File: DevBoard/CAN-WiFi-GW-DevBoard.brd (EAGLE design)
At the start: 82.5 x 58.4 mm, 31 parts, among them J1 IN+, J2 OUT+, J3 IN-, J4 OUT-, J5 CAN_MODULE, SW1 CONFIGURATION, U1 74LVC1T45GW,125, U2 74LVC1T45GW,125, U3 74LVC1T45GW,125, X1 MKDSN1,5/2-5,08

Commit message: Fix labelling of config switches
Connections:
- net ESP_D6/LISTEN_MODE renamed ESP_D6/CAN_TX_EN
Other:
- board text added: "1 OTA 2 WRITE 3 CANTX 4 DEBUG"
- board text removed: "1 OTA 2 WRITE 3 LISTEN 4 DEBUG"
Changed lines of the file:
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@@
 <text x="56.8325" y="33.655" size="1.016" layer="21" font="vector" rot="R90" align="top-left">1 OTA
 2 WRITE
-3 LISTEN
+3 CANTX
 4 DEBUG</text>
 <text x="15.02" y="51.34" size="1.27" layer="21" font="vector" align="center">[dev. board]</text>
@@
 <wire x1="28.3152125" y1="44.1325" x2="24.13" y2="39.9472875" width="0.2032" layer="16"/>
 </signal>
-<signal name="ESP_D6/LISTEN_MODE">
+<signal name="ESP_D6/CAN_TX_EN">
 <contactref element="J8" pad="7"/>
 <contactref element="SW1" pad="3"/>

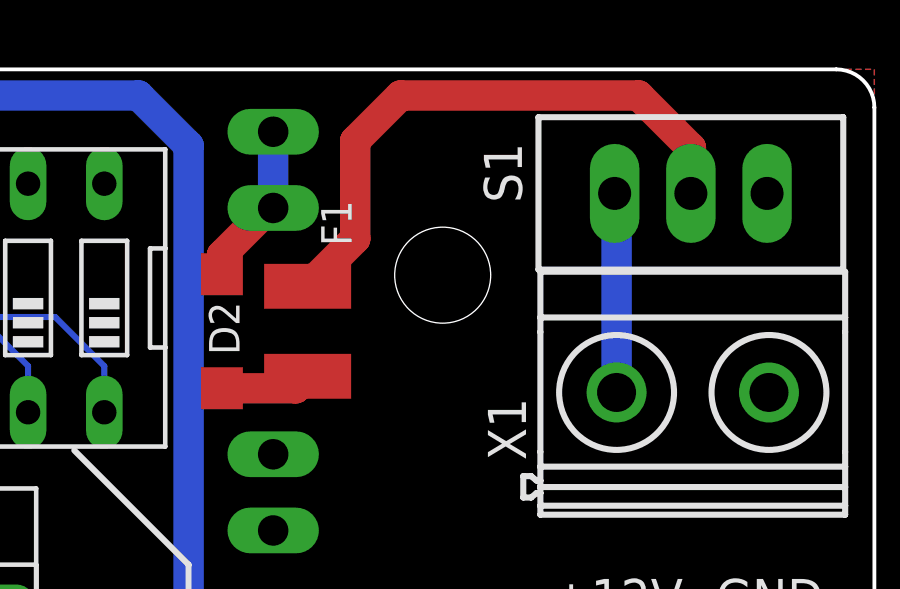
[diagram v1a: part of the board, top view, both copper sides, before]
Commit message: Remove redundant diode before power supply
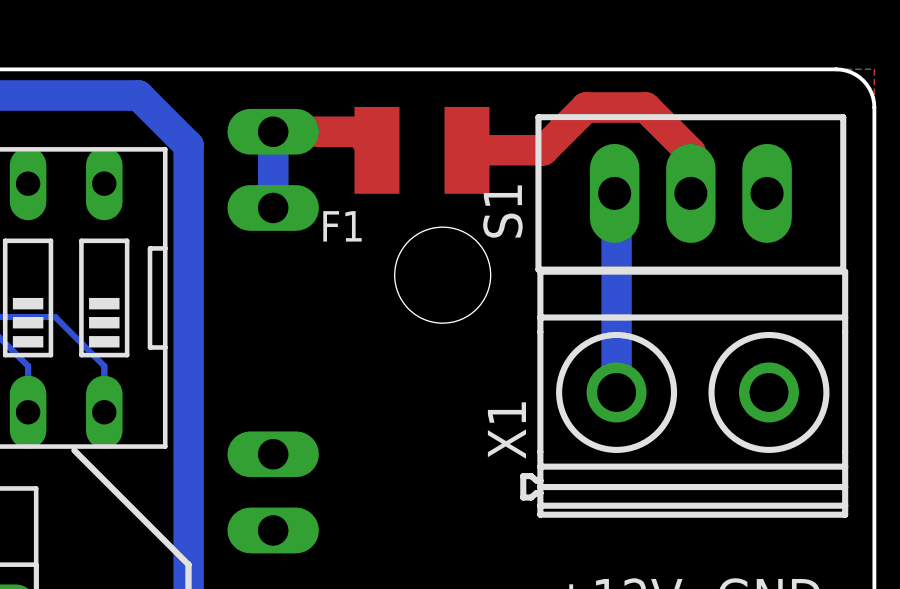
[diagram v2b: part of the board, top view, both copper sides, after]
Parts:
- removed D2: MBR0520LT, diode:SOD123
- moved F1 7.13 mm to (67.5, 55.7), turned to 180 degrees
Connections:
- removed net N$5: D2.A, F1.2
- net VIN: now also F1.2; no longer D2.C
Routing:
- net N$4: track 19.6 -> 10.0 mm
- net N$5: track 3.02 -> 0.00 mm
- net VIN: track 5.54 -> 6.26 mm
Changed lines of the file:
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@@
 </element>
 <element name="S1" library="switch" library_urn="urn:adsk.eagle:library:380" package="TL3XPO" package3d_urn="urn:adsk.eagle:package:27745/1" value="OFF/ON" x="76.4325" y="54.285" smashed="yes" grouprefs="POWER_SWITCH">
-<attribute name="NAME" x="70.8025" y="53.975" size="1.27" layer="25" ratio="10" rot="R90"/>
+<attribute name="NAME" x="70.8025" y="52.705" size="1.27" layer="25" ratio="10" rot="R90"/>
 <attribute name="POPULARITY" value="2" x="76.4325" y="54.285" size="1.778" layer="27" display="off"/>
 </element>
@@
 <attribute name="VALUE" x="56.44" y="4.445" size="1.27" layer="27"/>
 </element>
-<element name="F1" library="custom" package="FSMD050-1210-R" value="500mA" x="63.65875" y="49.68875" smashed="yes" rot="R270">
-<attribute name="NAME" x="65.125" y="52.53375" size="1.016" layer="25" rot="R90"/>
-</element>
-<element name="D2" library="diode" library_urn="urn:adsk.eagle:library:210" package="SOD123" package3d_urn="urn:adsk.eagle:package:43420/1" value="MBR0520LT" x="60.80125" y="49.68875" smashed="yes" rot="R270">
-<attribute name="NAME" x="61.38875" y="48.90625" size="1.016" layer="25" rot="R90"/>
-<attribute name="POPULARITY" value="2" x="60.80125" y="49.68875" size="1.778" layer="27" rot="R270" display="off"/>
+<element name="F1" library="custom" package="FSMD050-1210-R" value="500mA" x="67.46875" y="55.72125" smashed="yes" rot="R180">
+<attribute name="NAME" x="65.57625" y="53.695" size="1.016" layer="25" rot="R180"/>
 </element>
 </elements>
@@
 <contactref element="J1" pad="1"/>
 <wire x1="62.51" y1="56.34" x2="62.51" y2="53.8" width="1.016" layer="16"/>
-<contactref element="D2" pad="C"/>
-<wire x1="60.80125" y1="51.58875" x2="60.80125" y2="52.22875" width="1.016" layer="1"/>
-<wire x1="62.51" y1="53.8" x2="62.3725" y2="53.8" width="1.016" layer="1"/>
-<wire x1="62.3725" y1="53.8" x2="60.80125" y2="52.22875" width="1.016" layer="1"/>
+<contactref element="F1" pad="2"/>
+<wire x1="65.96875" y1="55.72125" x2="65.35" y2="56.34" width="1.016" layer="1"/>
+<wire x1="65.35" y1="56.34" x2="62.51" y2="56.34" width="1.016" layer="1"/>
 </signal>
 <signal name="+12V">
@@
 <contactref element="S1" pad="2"/>
 <contactref element="F1" pad="1"/>
-<wire x1="76.4325" y1="54.285" x2="76.4325" y2="55.80625" width="1.016" layer="1"/>
-<wire x1="76.4325" y1="55.80625" x2="74.69025" y2="57.5485" width="1.016" layer="1"/>
-<wire x1="74.69025" y1="57.5485" x2="66.756" y2="57.5485" width="1.016" layer="1"/>
-<wire x1="66.756" y1="57.5485" x2="65.24625" y2="56.03875" width="1.016" layer="1"/>
-<wire x1="65.24625" y1="56.03875" x2="65.24625" y2="52.77625" width="1.016" layer="1"/>
-<wire x1="65.24625" y1="52.77625" x2="63.65875" y2="51.18875" width="1.016" layer="1"/>
-</signal>
-<signal name="N$5">
-<contactref element="F1" pad="2"/>
-<contactref element="D2" pad="A"/>
-<wire x1="63.65875" y1="48.18875" x2="63.25875" y2="47.78875" width="1.016" layer="1"/>
-<wire x1="63.25875" y1="47.78875" x2="60.80125" y2="47.78875" width="1.016" layer="1"/>
+<wire x1="76.4325" y1="54.285" x2="76.4325" y2="55.6475" width="1.016" layer="1"/>
+<wire x1="76.4325" y1="55.6475" x2="74.93" y2="57.15" width="1.016" layer="1"/>
+<wire x1="74.93" y1="57.15" x2="72.9375" y2="57.15" width="1.016" layer="1"/>
+<wire x1="72.9375" y1="57.15" x2="71.50875" y2="55.72125" width="1.016" layer="1"/>
+<wire x1="71.50875" y1="55.72125" x2="68.96875" y2="55.72125" width="1.016" layer="1"/>
 </signal>
 <signal name="N$6">
